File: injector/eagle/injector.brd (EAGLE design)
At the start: 34 x 35.8 mm, 34 parts, among them J4 ICSP, U1 ATA6631, U2 ATMEGA328, U3 ATA6631, X1 16MHz

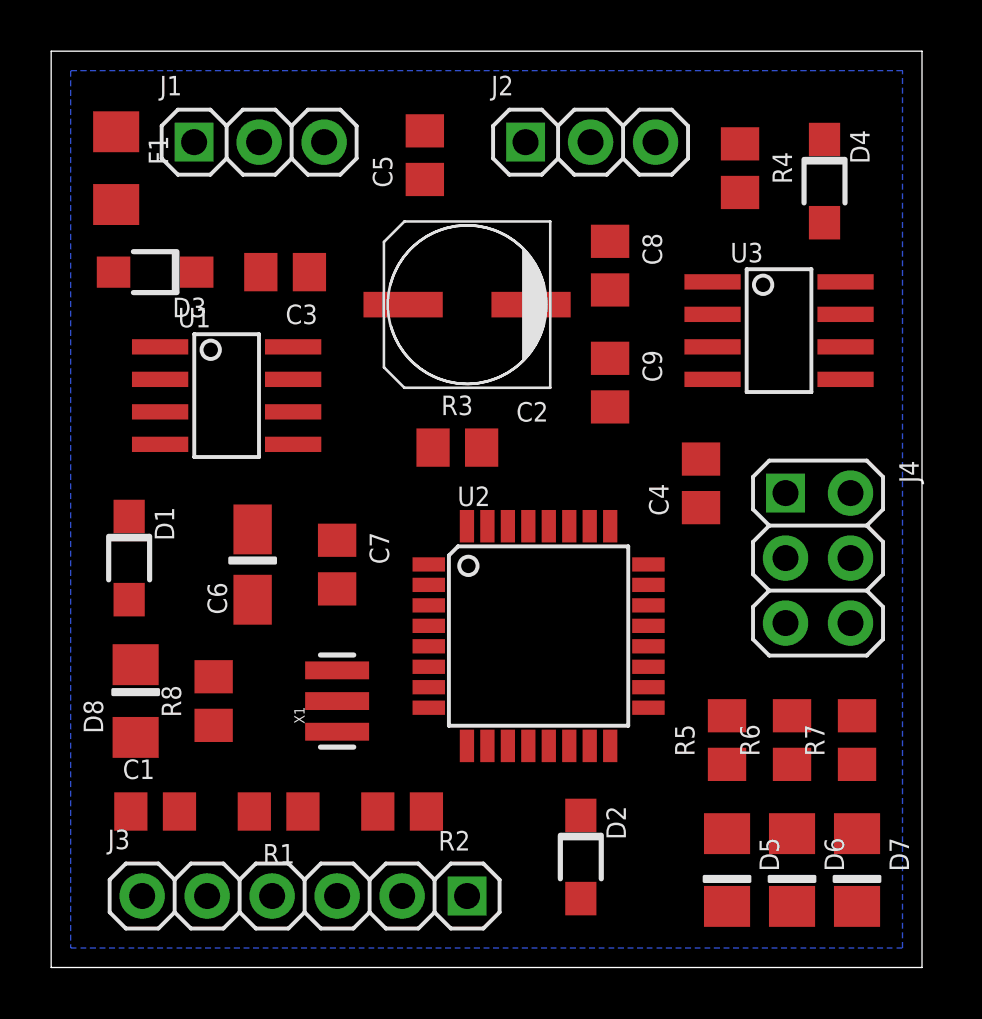
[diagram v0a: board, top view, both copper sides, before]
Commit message: Injector board is ready for auto routing.
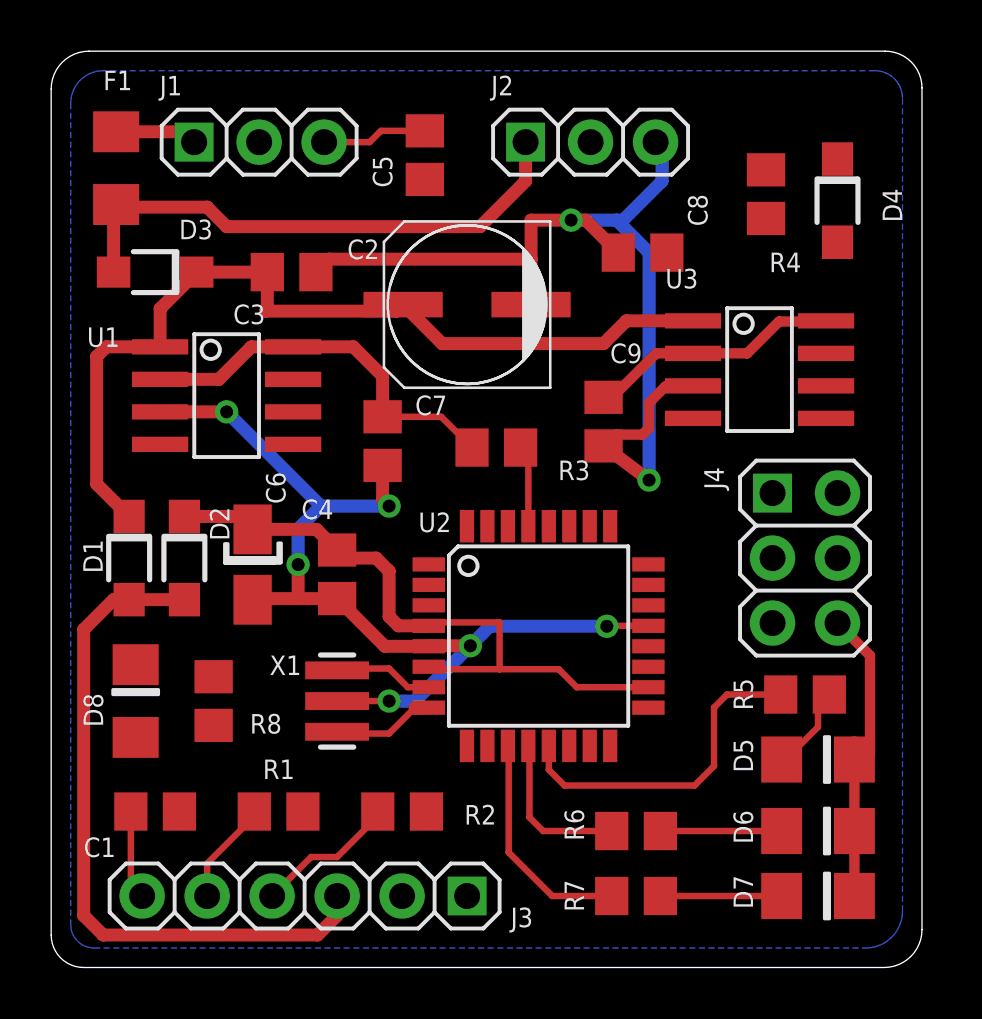
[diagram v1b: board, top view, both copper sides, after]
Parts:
- moved D2 19.4 mm to (5.21, 16.0)
- moved C4 14.7 mm to (11.2, 15.4), turned to 270 degrees
- moved R7 10.6 mm to (22.9, 2.79), turned to 180 degrees
- moved R6 7.06 mm to (22.9, 5.33), turned to 180 degrees
- moved D5 5.59 mm to (30.0, 8.13), turned to 0 degrees
- moved C7 5.14 mm to (13.0, 20.6)
- moved R5 3.53 mm to (29.5, 10.7), turned to 180 degrees
- moved D6 1.83 mm to (30.0, 5.33), turned to 0 degrees
- moved D7 1.83 mm to (30.0, 2.79), turned to 0 degrees
- moved U3 1.70 mm to (27.7, 23.4)
- moved C9 1.55 mm to (21.6, 21.3)
- moved R3 1.52 mm to (17.4, 20.3)
- moved R4 1.44 mm to (27.9, 30.2)
- moved C8 1.37 mm to (23.1, 27.9), turned to 180 degrees
- moved D4 0.92 mm to (30.7, 30.0)
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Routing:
- net GND: track 0.00 -> 94.2 mm, vias 0 -> 8
- net +5V: track 0.00 -> 41.5 mm
- net +12V: track 0.00 -> 35.0 mm
- net S-5V: track 0.00 -> 26.9 mm
- net N$6: track 0.00 -> 21.3 mm
- net ERROR_LED: track 0.00 -> 13.1 mm
- net SECONDARY_5V: track 0.00 -> 9.93 mm
- net STATUS_LED: track 0.00 -> 8.91 mm
- net FRAME_LED: track 0.00 -> 6.25 mm
- net TXO: track 0.00 -> 5.61 mm
- net N$3: track 0.00 -> 4.74 mm
- net N$1: track 0.00 -> 4.74 mm
- net RXI: track 0.00 -> 4.07 mm
- net XTAL2: track 0.00 -> 4.03 mm
- net XTAL1: track 0.00 -> 3.91 mm
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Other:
- outline, holes or cut-outs redrawn

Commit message: More layout tweaking before auto routing.
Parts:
- moved R2 0.36 mm to (14.0, 6.35)
- moved C1 0.36 mm to (4.32, 6.35)
- moved R1 0.36 mm to (9.14, 6.35)
- moved C8 0.25 mm to (23.1, 27.7)
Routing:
- net GND: track 94.2 -> 91.8 mm
- net TXO: track 5.61 -> 7.49 mm
- net RXI: track 4.07 -> 5.02 mm
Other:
- board text added: "12V"
- board text added: "5V"
- board text added: "CTS"
- board text added: "DTR"
- board text added: "GND"
- board text added: "ICSP"
- board text added: "LIN"
- board text added: "LINBUS INJECTOR REV A"
- board text added: "RX"
- board text added: "TO MASTER"
- board text added: "TO SLAVE"
- board text added: "TX"

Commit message: More pre autorouter tweaking.
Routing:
- net +5V: track 41.5 -> 47.5 mm
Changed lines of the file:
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@@
 </element>
 <element name="J4" library="injector" package="2X03" value="ICSP" x="29.464" y="16.002" smashed="yes" rot="R270">
-<attribute name="NAME" x="26.543" y="12.446" size="0.762" layer="25" ratio="10" rot="SR90"/>
+<attribute name="NAME" x="25.019" y="18.034" size="0.762" layer="25" ratio="10" rot="SR90"/>
 <attribute name="VALUE" x="25.019" y="19.812" size="1.27" layer="27" rot="R270"/>
 </element>
@@
 <wire x1="23.368" y1="19.05" x2="23.368" y2="27.686" width="0.508" layer="16"/>
 <wire x1="31.394" y1="8.788" x2="31.394" y2="8.128" width="0.508" layer="1"/>
-<wire x1="4.258" y1="21.717" x2="6.858" y2="21.717" width="0.508" layer="1"/>
-<via x="6.858" y="21.717" extent="1-16" drill="0.508"/>
-<wire x1="6.858" y1="21.717" x2="10.541" y2="18.034" width="0.508" layer="16"/>
+<wire x1="4.258" y1="21.717" x2="6.096" y2="21.717" width="0.508" layer="1"/>
+<via x="6.096" y="21.717" extent="1-16" drill="0.508"/>
+<wire x1="6.096" y1="21.717" x2="10.541" y2="18.034" width="0.508" layer="16"/>
 <wire x1="10.541" y1="18.034" x2="13.208" y2="18.034" width="0.508" layer="16"/>
 <via x="13.208" y="18.034" extent="1-16" drill="0.508"/>
@@
 <wire x1="23.368" y1="30.48" x2="23.622" y2="30.734" width="0.508" layer="16"/>
 <wire x1="23.622" y1="30.734" x2="23.622" y2="32.258" width="0.508" layer="16"/>
-<wire x1="18.756" y1="27.686" x2="20.32" y2="27.686" width="0.508" layer="1"/>
+<wire x1="18.756" y1="27.686" x2="20.574" y2="27.686" width="0.508" layer="1"/>
 <wire x1="20.574" y1="27.686" x2="22.164" y2="27.686" width="0.508" layer="1"/>
 <wire x1="23.368" y1="30.48" x2="23.368" y2="27.686" width="0.508" layer="16"/>
 <wire x1="23.368" y1="27.686" x2="20.574" y2="27.686" width="0.508" layer="16"/>
 <via x="20.574" y="27.686" extent="1-16" drill="0.508"/>
-<wire x1="20.574" y1="27.686" x2="20.32" y2="27.686" width="0.508" layer="1"/>
-<wire x1="10.856" y1="27.686" x2="10.668" y2="32.258" width="0" layer="19" extent="1-1"/>
-<wire x1="23.3426" y1="13.354" x2="23.368" y2="19.05" width="0" layer="19" extent="1-1"/>
+<wire x1="32.004" y1="8.382" x2="31.394" y2="8.128" width="0" layer="19" extent="1-1"/>
 <wire x1="14.7574" y1="14.154" x2="14.7764" y2="12.573" width="0" layer="19" extent="1-1"/>
 <wire x1="3.302" y1="11.836" x2="7.874" y2="14.373" width="0" layer="19" extent="1-1"/>
-<wire x1="30.734" y1="13.462" x2="23.3426" y2="13.354" width="0" layer="19" extent="1-1"/>
-<wire x1="31.394" y1="8.128" x2="32.004" y2="8.382" width="0" layer="19" extent="1-1"/>
-<wire x1="13.716" y1="2.794" x2="13.208" y2="10.414" width="0" layer="19" extent="1-1"/>
-<wire x1="16.256" y1="2.794" x2="13.716" y2="2.794" width="0" layer="19" extent="1-1"/>
 </signal>
 <signal name="N$3">
@@
 <wire x1="16.449" y1="20.32" x2="15.245" y2="21.524" width="0.254" layer="1"/>
 <wire x1="15.245" y1="21.524" x2="12.954" y2="21.524" width="0.254" layer="1"/>
-<wire x1="4.258" y1="22.987" x2="4.385" y2="23.114" width="0.254" layer="1"/>
 <wire x1="14.7574" y1="11.754" x2="14.8528" y2="11.6586" width="0.254" layer="1"/>
 <wire x1="14.8528" y1="11.6586" x2="17.526" y2="11.6586" width="0.254" layer="1"/>
@@
 <wire x1="19.8374" y1="11.6586" x2="20.542" y2="10.954" width="0.254" layer="1"/>
 <wire x1="20.542" y1="10.954" x2="23.3426" y2="10.954" width="0.254" layer="1"/>
-<wire x1="9.458" y1="24.257" x2="7.8232" y2="24.257" width="0.508" layer="1"/>
-<wire x1="7.8232" y1="24.257" x2="6.5532" y2="22.987" width="0.508" layer="1"/>
-<wire x1="6.5532" y1="22.987" x2="4.258" y2="22.987" width="0.508" layer="1"/>
+<wire x1="9.458" y1="24.257" x2="7.62" y2="24.257" width="0.508" layer="1"/>
+<wire x1="7.62" y1="24.257" x2="7.62" y2="22.987" width="0.508" layer="1"/>
+<wire x1="7.62" y1="22.987" x2="7.62" y2="17.526" width="0.508" layer="1"/>
+<wire x1="4.258" y1="22.987" x2="7.62" y2="22.987" width="0.508" layer="1"/>
 <wire x1="23.3426" y1="10.954" x2="30.734" y2="18.542" width="0" layer="19" extent="1-1"/>
-<wire x1="12.954" y1="21.524" x2="10.37" y2="17.123" width="0" layer="19" extent="1-1"/>
+<wire x1="7.62" y1="17.526" x2="7.37" y2="17.627" width="0" layer="19" extent="1-1"/>
 <wire x1="6.35" y1="11.364" x2="7.874" y2="17.123" width="0" layer="19" extent="1-1"/>
 </signal>

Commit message: All nets are routed.
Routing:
- net LIN1: track 0.00 -> 37.1 mm
- net RESET: track 3.37 -> 33.9 mm, vias 0 -> 2
- net +5V: track 47.5 -> 72.2 mm, vias 0 -> 1
- net LIN2: track 0.00 -> 19.0 mm, vias 0 -> 2
- net LIN2_TX: track 0.00 -> 18.8 mm, vias 0 -> 2
- net LIN1_TX: track 0.00 -> 17.8 mm, vias 0 -> 2
- net SER_TX: track 0.00 -> 17.6 mm, vias 0 -> 2
- net MOSI/LIN_ERR: track 0.00 -> 16.6 mm, vias 0 -> 2
- net MISO/LIN_DATA: track 0.00 -> 13.3 mm, vias 0 -> 2
- net SER_RX: track 0.00 -> 12.5 mm, vias 0 -> 2
- net LIN2_RX: track 0.00 -> 9.32 mm
- net LIN1_RX: track 0.00 -> 9.18 mm, vias 0 -> 2
- net SCK: track 0.00 -> 9.06 mm
- net +12V: track 35.0 -> 43.1 mm
- net GND: track 91.6 -> 98.8 mm, vias 8 -> 9
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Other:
- board text added: "LINBUS INJECTOR - REV A"

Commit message: Tweaked the board layout.
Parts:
- moved D5 0.25 mm to (30.0, 7.87)
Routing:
- net GND: track 98.8 -> 98.1 mm
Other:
- board text added: "ER"
- board text added: "FR"
- board text added: "ST"
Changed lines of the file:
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@@
 <text x="21.844" y="30.734" size="0.762" layer="21" rot="SR180">LIN</text>
 <text x="24.892" y="30.734" size="0.762" layer="21" rot="SR180">GND</text>
-<text x="23.876" y="29.718" size="0.762" layer="21" rot="SR180">TO SLAVE</text>
-<text x="11.176" y="29.718" size="0.762" layer="21" rot="SR180">TO MASTER</text>
+<text x="24.892" y="29.718" size="0.762" layer="21" rot="SR180">TO SLAVE</text>
+<text x="11.684" y="29.718" size="0.762" layer="21" rot="SR180">TO MASTER</text>
 <text x="26.416" y="14.732" size="0.762" layer="21" rot="SR90">ICSP</text>
 <wire x1="26.162" y1="18.796" x2="26.162" y2="18.542" width="0.2032" layer="21"/>
@@
 <text x="0.762" y="24.13" size="0.762" layer="21" rot="SR270">LINBUS INJECTOR REV A</text>
 <text x="1.016" y="28.321" size="1.016" layer="30" font="vector" ratio="15" rot="SMR90" align="bottom-right">LINBUS INJECTOR - REV A</text>
+<text x="26.162" y="7.112" size="0.762" layer="21" rot="SR90">ER</text>
+<text x="26.162" y="4.572" size="0.762" layer="21" rot="SR90">FR</text>
+<text x="26.162" y="2.032" size="0.762" layer="21" rot="SR90">ST</text>
 </plain>
 <attributes>
@@
 </element>
 <element name="C3" library="injector" package="C0805" value="0.1uF 40V" x="9.398" y="27.178" smashed="yes">
-<attribute name="NAME" x="12.446" y="27.432" size="0.762" layer="25" rot="R90"/>
+<attribute name="NAME" x="8.128" y="26.162" size="0.762" layer="25" rot="R180"/>
 <attribute name="VALUE" x="8.128" y="24.638" size="1.27" layer="27"/>
 </element>
 <element name="C2" library="injector" package="UD-6,3X5,8_NICHICON" value="22uF 40V" x="16.256" y="25.908" smashed="yes" rot="R180">
-<attribute name="NAME" x="21.209" y="24.638" size="0.762" layer="25" rot="R180"/>
+<attribute name="NAME" x="19.812" y="25.019" size="0.762" layer="25" rot="R270"/>
 <attribute name="VALUE" x="19.431" y="30.353" size="1.016" layer="27" rot="R180"/>
 </element>
@@
 </element>
 <element name="U3" library="injector" package="SO-08" value="ATA6631" x="27.686" y="23.368" smashed="yes" rot="R270">
-<attribute name="NAME" x="21.717" y="25.527" size="0.762" layer="25"/>
+<attribute name="NAME" x="22.225" y="24.511" size="0.762" layer="25"/>
 <attribute name="VALUE" x="25.781" y="19.431" size="1.27" layer="27"/>
 </element>
@@
 <attribute name="VALUE" x="16.764" y="17.78" size="1.27" layer="27"/>
 </element>
-<element name="D5" library="injector" package="1206-LED" value="" x="29.972" y="8.128" smashed="yes">
-<attribute name="NAME" x="27.178" y="7.62" size="0.762" layer="25" rot="R90"/>
-<attribute name="VALUE" x="28.702" y="5.588" size="1.27" layer="27"/>
+<element name="D5" library="injector" package="1206-LED" value="" x="29.972" y="7.874" smashed="yes">
+<attribute name="NAME" x="27.178" y="7.112" size="0.762" layer="25" rot="R90"/>
+<attribute name="VALUE" x="28.702" y="5.334" size="1.27" layer="27"/>
 </element>
 <element name="D6" library="injector" package="1206-LED" value="" x="29.972" y="5.334" smashed="yes">
-<attribute name="NAME" x="27.178" y="4.826" size="0.762" layer="25" rot="R90"/>
+<attribute name="NAME" x="27.178" y="4.572" size="0.762" layer="25" rot="R90"/>
 <attribute name="VALUE" x="28.702" y="2.794" size="1.27" layer="27"/>
 </element>
@@
 </element>
 <element name="D7" library="injector" package="1206-LED" value="" x="29.972" y="2.794" smashed="yes">
-<attribute name="NAME" x="27.178" y="2.286" size="0.762" layer="25" rot="R90"/>
+<attribute name="NAME" x="27.178" y="2.032" size="0.762" layer="25" rot="R90"/>
 <attribute name="VALUE" x="28.702" y="0.254" size="1.27" layer="27"/>
 </element>
@@
 <via x="23.368" y="19.05" extent="1-16" drill="0.508"/>
 <wire x1="23.368" y1="19.05" x2="23.368" y2="27.686" width="0.508" layer="16"/>
-<wire x1="31.394" y1="8.788" x2="31.394" y2="8.128" width="0.508" layer="1"/>
+<wire x1="31.394" y1="7.772" x2="31.394" y2="7.874" width="0.508" layer="1"/>
 <wire x1="4.258" y1="21.717" x2="6.096" y2="21.717" width="0.508" layer="1"/>
 <via x="6.096" y="21.717" extent="1-16" drill="0.508"/>
@@
 <wire x1="10.856" y1="27.686" x2="18.756" y2="27.686" width="0.508" layer="1"/>
 <wire x1="31.394" y1="2.794" x2="31.394" y2="5.334" width="0.4064" layer="1"/>
-<wire x1="31.394" y1="8.128" x2="31.394" y2="5.334" width="0.4064" layer="1"/>
+<wire x1="31.394" y1="7.772" x2="31.394" y2="5.334" width="0.4064" layer="1"/>
 <wire x1="30.734" y1="13.462" x2="32.004" y2="12.192" width="0.4064" layer="1"/>
 <wire x1="32.004" y1="12.192" x2="32.004" y2="8.4582" width="0.4064" layer="1"/>
@@
 <wire x1="3.302" y1="10.4394" x2="3.302" y2="11.836" width="0.254" layer="1"/>
 <wire x1="32.004" y1="8.4582" x2="31.623" y2="8.4582" width="0.254" layer="1"/>
-<wire x1="31.623" y1="8.4582" x2="31.394" y2="8.128" width="0.254" layer="1"/>
+<wire x1="31.623" y1="8.4582" x2="31.394" y2="7.874" width="0.254" layer="1"/>
 <via x="3.302" y="10.4394" extent="1-16" drill="0.3302"/>
 <wire x1="16.383" y1="12.573" x2="16.891" y2="12.573" width="0.254" layer="16"/>
@@
 <wire x1="29.972" y1="10.226" x2="29.972" y2="9.398" width="0.254" layer="1"/>
 <wire x1="29.972" y1="9.398" x2="28.702" y2="8.128" width="0.254" layer="1"/>
-<wire x1="28.702" y1="8.128" x2="28.55" y2="8.128" width="0.254" layer="1"/>
+<wire x1="28.702" y1="8.128" x2="28.55" y2="7.874" width="0.254" layer="1"/>
 </signal>
 <signal name="LIN1">
